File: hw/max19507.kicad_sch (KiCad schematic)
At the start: 43 parts, among them U8 THS4522, U9 MAX19517

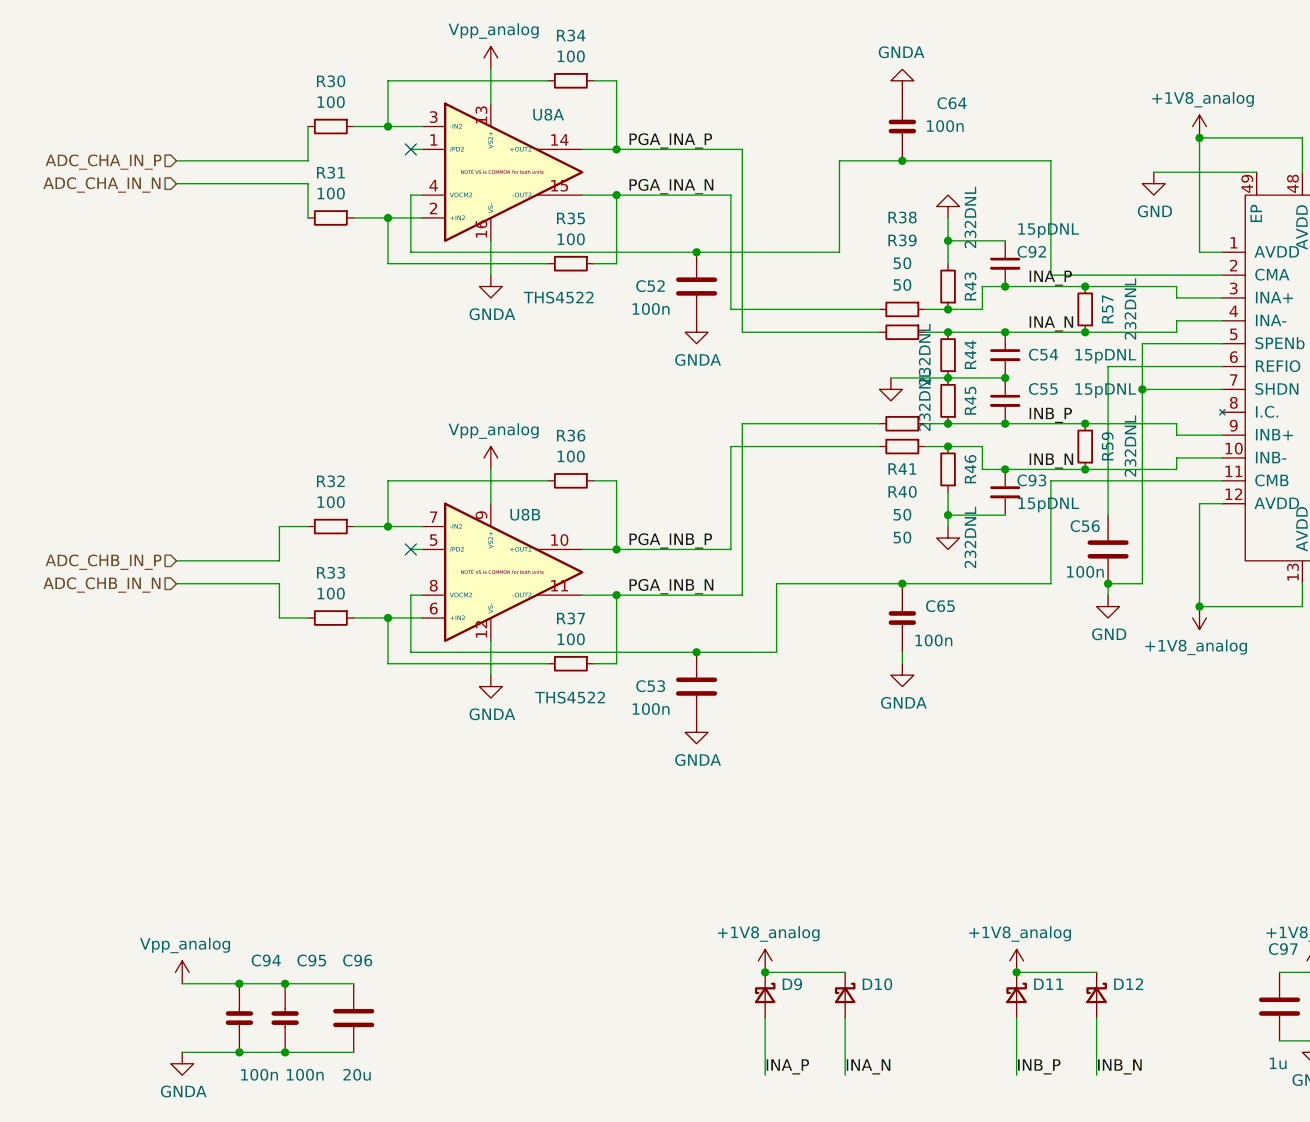
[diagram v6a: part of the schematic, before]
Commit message: removed THS4255
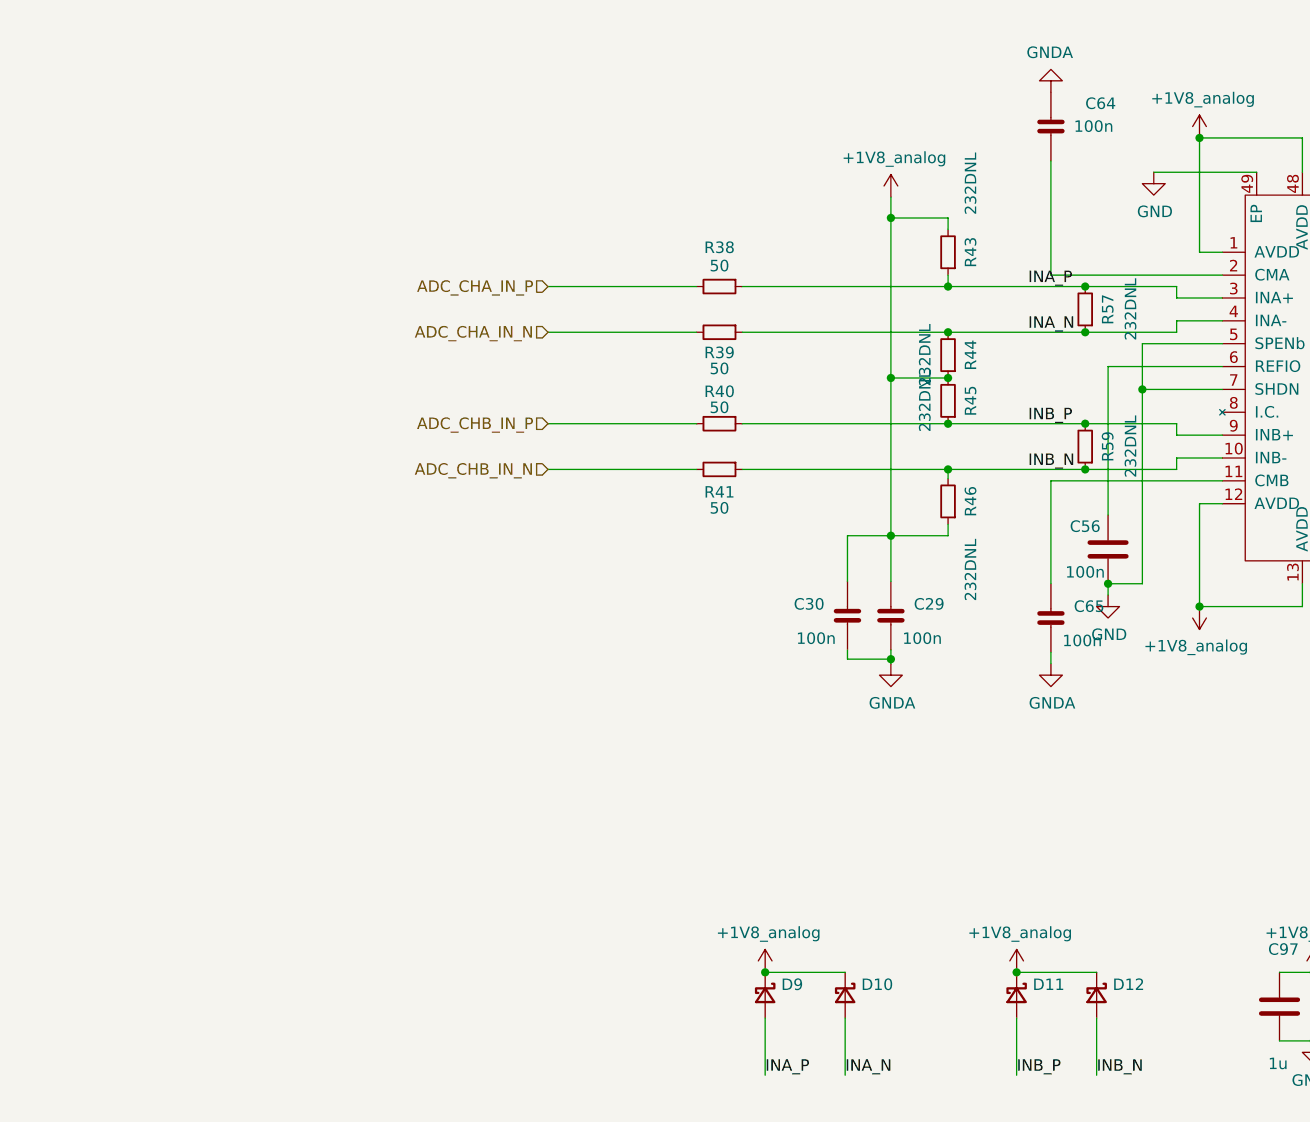
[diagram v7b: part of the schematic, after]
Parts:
- removed C52, C53: 100n, Capacitor_SMD:C_0603_1608Metric, symbol fmc:100nF_603
- removed C54, C55, C92, C93: 15pDNL, Capacitor_SMD:C_0603_1608Metric, symbol Device:C_Small
- removed C94, C95: 100n, Capacitor_SMD:C_0603_1608Metric, symbol fmc:100nF_402
- removed C96: 20u, Capacitor_SMD:C_0805_2012Metric, symbol fmc:1uF_805
- removed R30, R31, R32, R33: 100, Resistor_SMD:R_0402_1005Metric, symbol Device:R_Small
- removed R34, R35, R36, R37: 100, Resistor_SMD:R_0603_1608Metric, symbol Device:R_Small
- removed U8: THS4522, Package_SO:TSSOP-16_4.4x5mm_P0.65mm, symbol fmc:THS4522
- added C29, C30: 100n, Capacitor_SMD:C_0603_1608Metric, symbol fmc:100nF_402
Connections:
- net PGA_INA_N is gone; now on net ADC_CHA_IN_P: R38.2
- net PGA_INA_P is gone; now on net ADC_CHA_IN_N: R39.2
- net PGA_INB_N is gone; now on net ADC_CHB_IN_P: R40.2
- net PGA_INB_P is gone; now on net ADC_CHB_IN_N: R41.2
- net +1V8_analog: now also R43.2, R44.1, R45.2, R46.1, C29.1, C30.1
- net GND: no longer R43.2, R44.1, R45.2, R46.1
- net GNDA: now also C29.2, C30.2
- no-connect marks 14 -> 12
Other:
- moved on the sheet: C64, C65, R38, R39, R40, R41, R43, R46

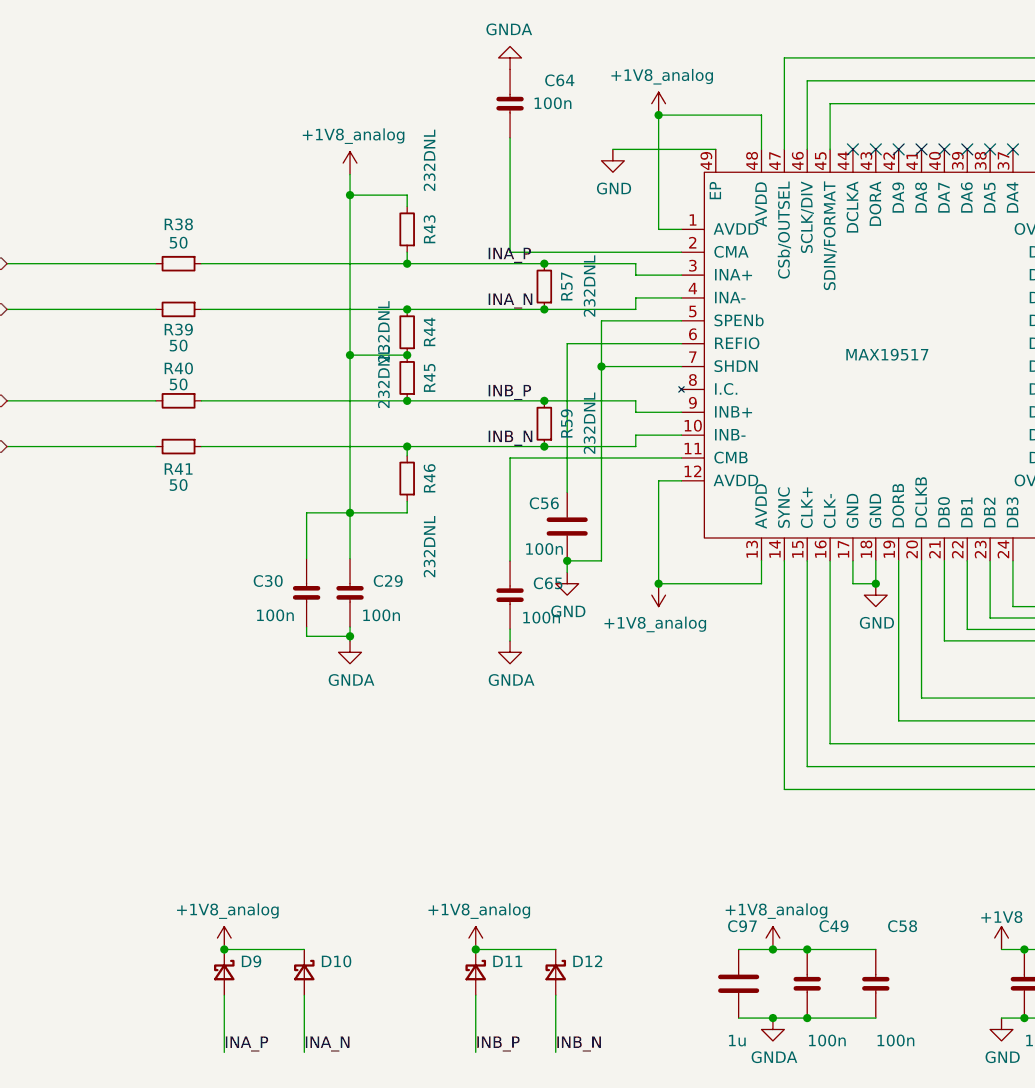
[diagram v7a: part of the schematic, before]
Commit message: rewired 1V8_analog to +2V5_analog
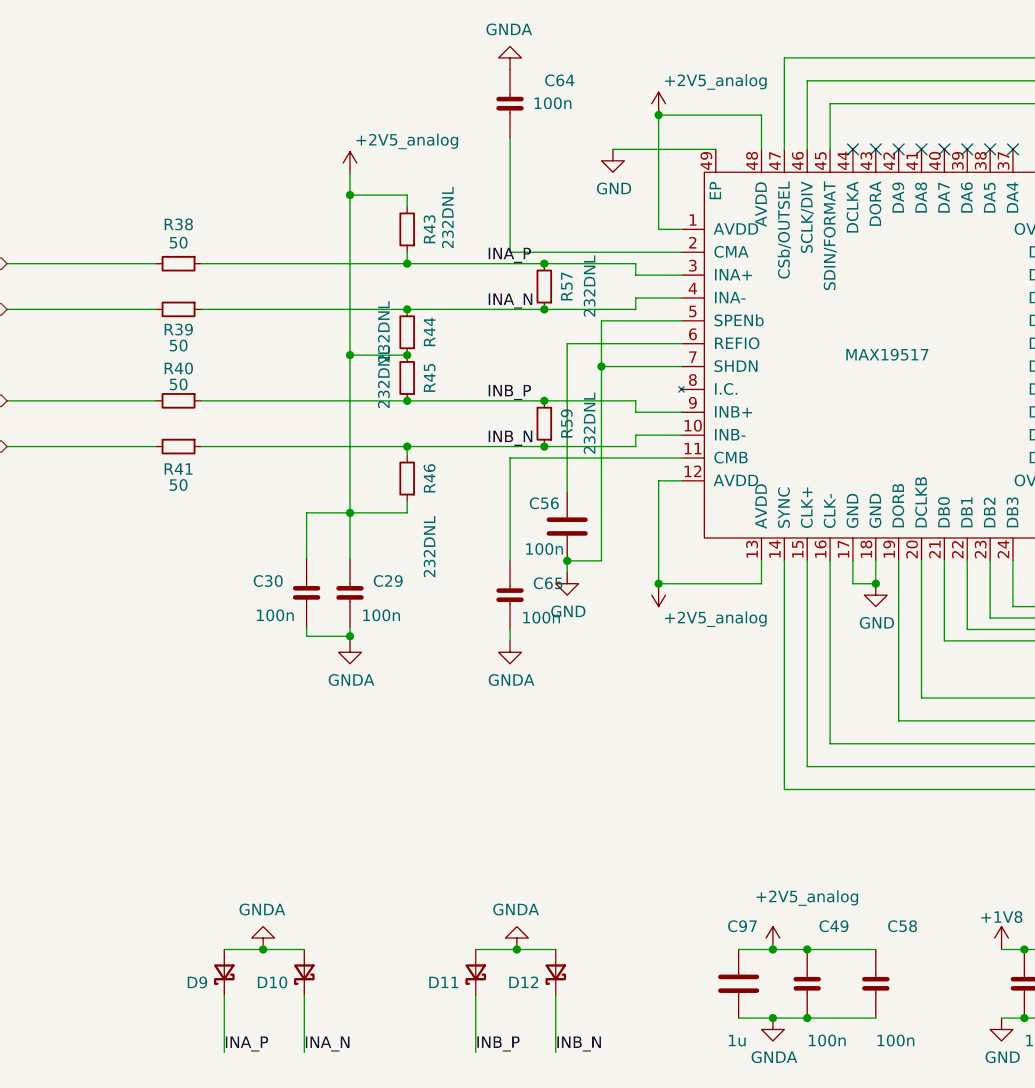
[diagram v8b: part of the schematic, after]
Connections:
- net GNDA: now also D10.2 (A), D11.2 (A), D12.2 (A), D9.2 (A)
- net INA_N: now also D10.1 (K); no longer D10.2 (A)
- net INA_P: now also D9.1 (K); no longer D9.2 (A)
- net INB_N: now also D12.1 (K); no longer D12.2 (A)
- net INB_P: now also D11.1 (K); no longer D11.2 (A)
- net +1V8_analog renamed +2V5_analog
- net +2V5_analog: no longer D10.1 (K), D11.1 (K), D12.1 (K), D9.1 (K)
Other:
- moved on the sheet: D10, D11, D12, D9
